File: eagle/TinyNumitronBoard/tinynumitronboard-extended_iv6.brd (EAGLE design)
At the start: 100 x 50 mm, 34 parts

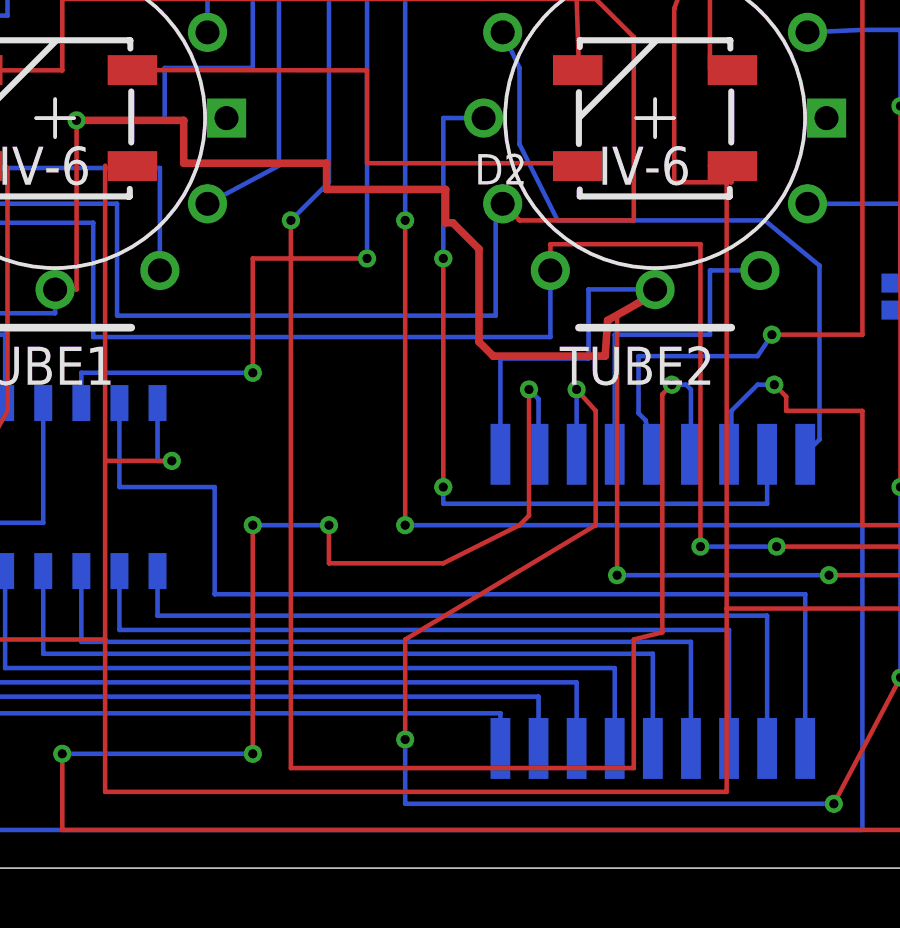
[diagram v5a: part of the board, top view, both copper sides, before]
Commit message: Wiring finished, DRC ok
Before last run of script
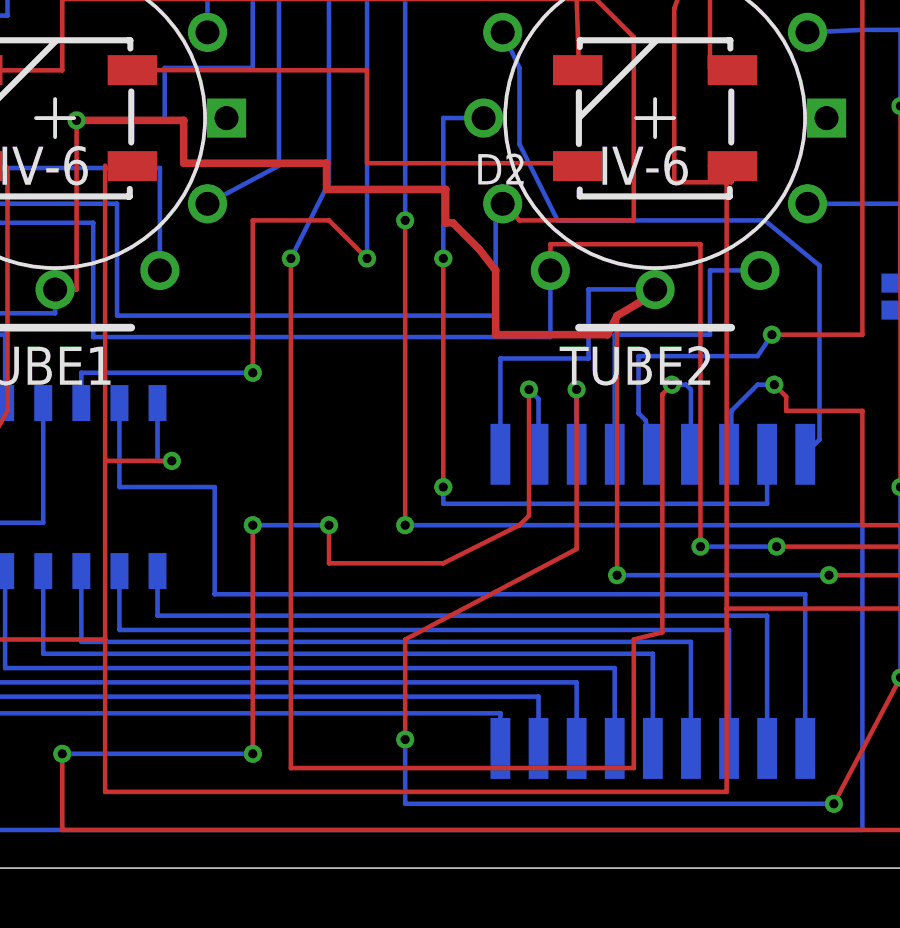
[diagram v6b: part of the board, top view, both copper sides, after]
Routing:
- net N$23: track 48.2 -> 50.0 mm
- net GRID_P: track 186.7 -> 185.2 mm
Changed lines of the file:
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@@
 <wire x1="25.4" y1="33.416875" x2="25.4" y2="33.02" width="0.1524" layer="1"/>
 <wire x1="25.4" y1="33.02" x2="25.4" y2="20.32" width="0.1524" layer="16"/>
-<wire x1="25.4" y1="20.32" x2="21.59" y2="20.32" width="0.1524" layer="1"/>
-<wire x1="21.59" y1="20.32" x2="21.59" y2="16.51" width="0.1524" layer="1"/>
+<wire x1="25.4" y1="20.32" x2="24.13" y2="21.59" width="0.1524" layer="1"/>
+<wire x1="24.13" y1="21.59" x2="21.59" y2="21.59" width="0.1524" layer="1"/>
+<wire x1="21.59" y1="21.59" x2="21.59" y2="16.51" width="0.1524" layer="1"/>
 <wire x1="21.59" y1="16.51" x2="15.875" y2="16.51" width="0.1524" layer="16"/>
 <wire x1="15.875" y1="16.51" x2="15.875" y2="15.5" width="0.1524" layer="16"/>
@@
 <wire x1="26.67" y1="2.143125" x2="26.67" y2="4.28625" width="0.1524" layer="16"/>
 <wire x1="26.67" y1="4.28625" x2="26.67" y2="7.62" width="0.1524" layer="1"/>
-<wire x1="26.67" y1="7.62" x2="33.02" y2="11.43" width="0.1524" layer="1"/>
-<wire x1="33.02" y1="11.43" x2="33.02" y2="15.24" width="0.1524" layer="1"/>
-<wire x1="33.02" y1="15.24" x2="32.385" y2="15.954375" width="0.1524" layer="1"/>
+<wire x1="26.67" y1="7.62" x2="32.385" y2="10.63625" width="0.1524" layer="1"/>
+<wire x1="32.385" y1="10.63625" x2="32.385" y2="15.954375" width="0.1524" layer="1"/>
 <wire x1="32.385" y1="15.954375" x2="32.385" y2="13.7922" width="0.1524" layer="16"/>
 <via x="32.385" y="15.954375" extent="1-16" drill="0.3048"/>
@@
 <wire x1="28.019375" y1="21.510625" x2="28.2575" y2="21.510625" width="0.254" layer="1"/>
 <wire x1="28.2575" y1="21.510625" x2="29.130625" y2="20.6375" width="0.254" layer="1"/>
-<wire x1="29.130625" y1="20.6375" x2="29.130625" y2="17.541875" width="0.254" layer="1"/>
-<wire x1="29.130625" y1="17.541875" x2="29.606875" y2="17.065625" width="0.254" layer="1"/>
-<wire x1="29.606875" y1="17.065625" x2="33.3375" y2="17.065625" width="0.254" layer="1"/>
-<wire x1="33.3375" y1="17.065625" x2="33.416875" y2="18.25625" width="0.254" layer="1"/>
-<wire x1="33.416875" y1="18.25625" x2="34.686875" y2="18.970625" width="0.254" layer="1"/>
+<wire x1="29.130625" y1="20.6375" x2="29.68625" y2="19.923125" width="0.254" layer="1"/>
+<wire x1="29.68625" y1="19.923125" x2="29.68625" y2="17.78" width="0.254" layer="1"/>
+<wire x1="29.68625" y1="17.78" x2="33.416875" y2="17.78" width="0.254" layer="1"/>
+<wire x1="33.416875" y1="17.78" x2="33.734375" y2="18.415" width="0.254" layer="1"/>
+<wire x1="33.734375" y1="18.415" x2="34.686875" y2="18.970625" width="0.254" layer="1"/>
 <wire x1="34.686875" y1="18.970625" x2="35.004375" y2="19.288125" width="0.254" layer="1"/>
 <wire x1="2.54" y1="27.94" x2="6.0325" y2="27.94" width="0.1524" layer="16"/>
@@
 <wire x1="35" y1="19.285" x2="35.004375" y2="19.288125" width="0" layer="19" extent="1-1"/>
 <wire x1="15" y1="19.285" x2="15.001875" y2="19.288125" width="0" layer="19" extent="1-1"/>
-<wire x1="29.845" y1="13.7922" x2="29.606875" y2="17.065625" width="0" layer="19" extent="1-16"/>
+<wire x1="29.845" y1="13.7922" x2="29.68625" y2="17.78" width="0" layer="19" extent="1-16"/>
 </signal>
 <signal name="FIL_P">
@@
 <wire x1="30.48" y1="30.48" x2="24.13" y2="30.48" width="0.1524" layer="1"/>
 <wire x1="24.13" y1="30.48" x2="24.13" y2="22.86" width="0.1524" layer="16"/>
-<wire x1="24.13" y1="22.86" x2="22.86" y2="21.59" width="0.1524" layer="16"/>
-<wire x1="22.86" y1="21.59" x2="22.86" y2="3.33375" width="0.1524" layer="1"/>
+<wire x1="24.13" y1="22.86" x2="22.86" y2="20.32" width="0.1524" layer="16"/>
+<wire x1="22.86" y1="20.32" x2="22.86" y2="3.33375" width="0.1524" layer="1"/>
 <wire x1="22.86" y1="3.33375" x2="34.29" y2="3.33375" width="0.1524" layer="1"/>
 <wire x1="34.29" y1="3.33375" x2="34.29" y2="7.62" width="0.1524" layer="1"/>
@@
 <wire x1="36.195" y1="15.954375" x2="36.195" y2="13.731875" width="0.1524" layer="16"/>
 <via x="35.56" y="16.113125" extent="1-16" drill="0.3048"/>
-<via x="22.86" y="21.59" extent="1-16" drill="0.3048"/>
+<via x="22.86" y="20.32" extent="1-16" drill="0.3048"/>
 <via x="24.13" y="30.48" extent="1-16" drill="0.3048"/>
 </signal>

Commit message: Final commit before sending v2.0 to production
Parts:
- J_LED_IN, J_LED_OUT: device SparkFun-Connectors:1X01NS-KIT -> SparkFun-Connectors:1X01
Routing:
- net N$43: track 0.00 -> 84.7 mm, vias 0 -> 6
- net N$20: track 84.7 -> 0.00 mm, vias 6 -> 0
- net N$21: track 63.0 -> 0.00 mm, vias 3 -> 0
- net N$39: track 0.00 -> 62.9 mm, vias 0 -> 3
- net N$17: track 0.00 -> 42.1 mm, vias 0 -> 2
- net N$83: track 42.1 -> 0.00 mm, vias 2 -> 0
- net N$65: track 0.00 -> 17.8 mm
- net N$88: track 17.7 -> 0.00 mm
- net SER: vias 2 -> 1
- added copper zone on layer 16, net GND
